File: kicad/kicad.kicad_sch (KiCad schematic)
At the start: 41 parts, among them Q1 C945, Q2 C945, Q3 C945, Q4 C945, SW1 Mode_Push, SW2 Reset, U2 KW4-56NXLB-P, U3 74HC595, U4 STM32F072CBT6, Y1 8MHz

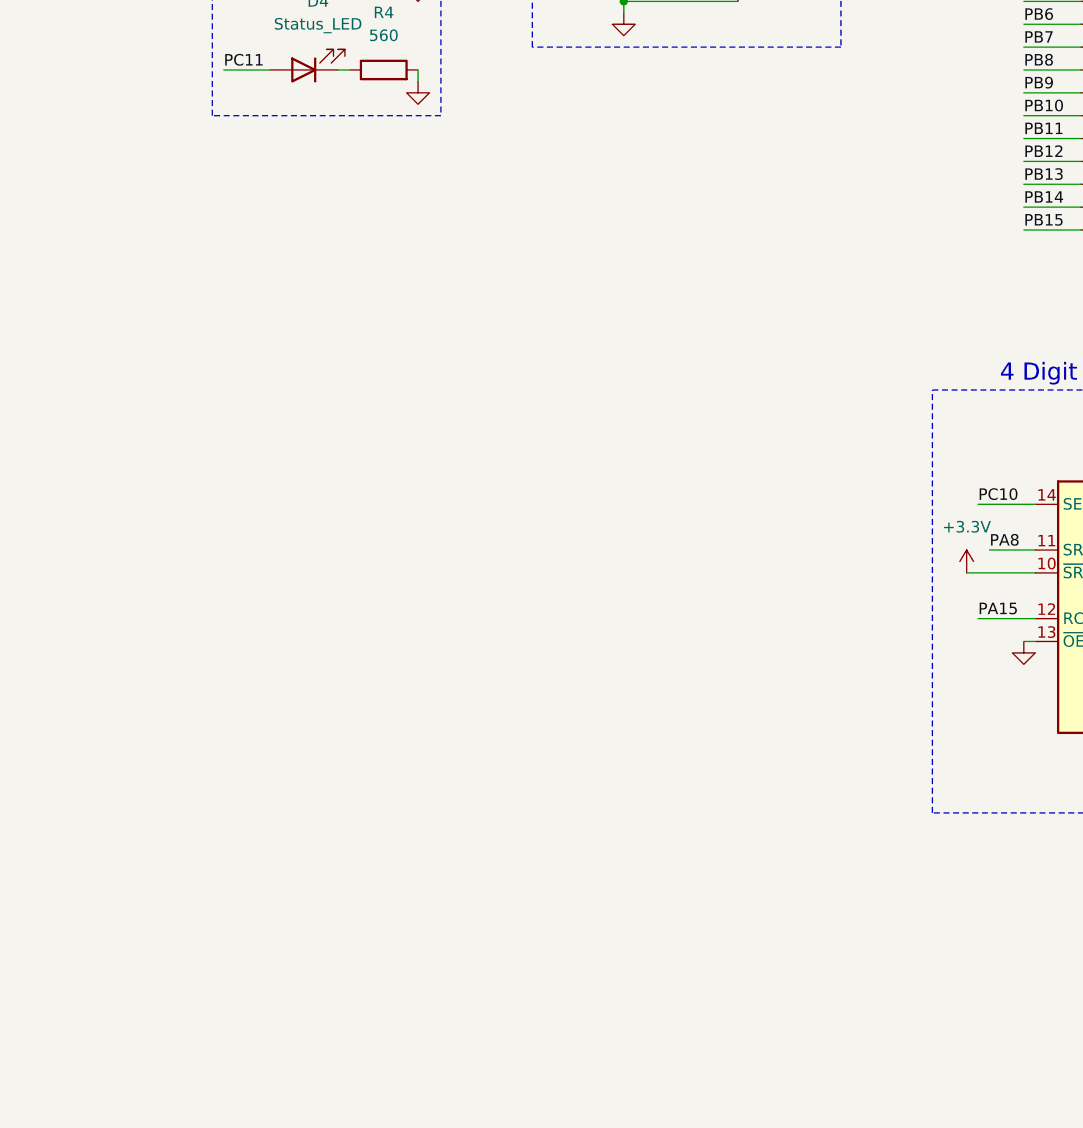
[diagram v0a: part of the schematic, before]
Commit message: add hall sensor
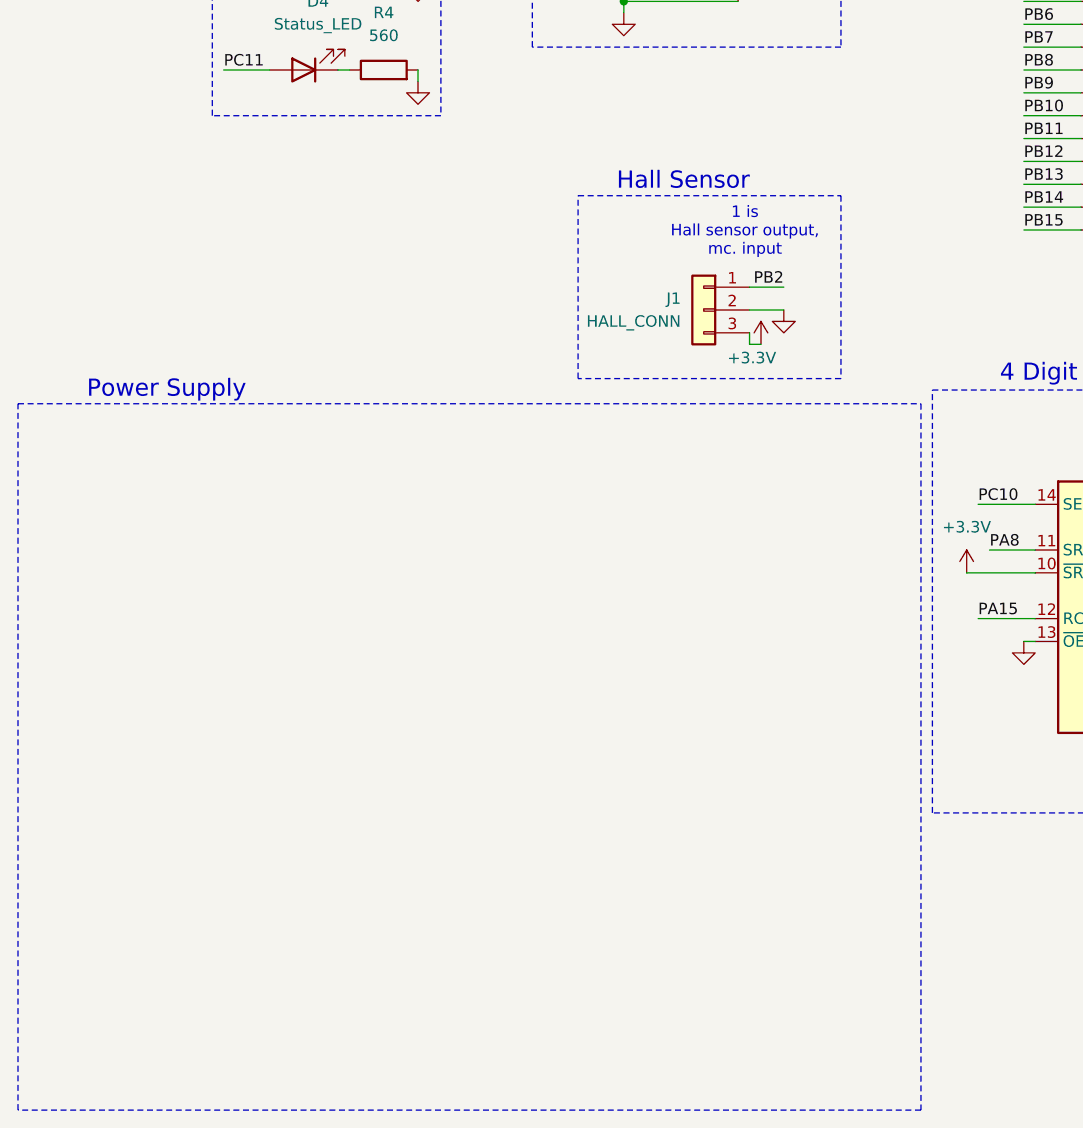
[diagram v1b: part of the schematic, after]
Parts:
- added J1: HALL_CONN, symbol Connector_Generic:Conn_01x03
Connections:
- net +3.3V: now also J1.3 (Pin_3)
- net GND: now also J1.2 (Pin_2)
- net PB2: now also J1.1 (Pin_1)
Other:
- note added: "1 is Hall sensor output, mc. input"
- note added: "Hall Sensor"
- note added: "Power Supply"
